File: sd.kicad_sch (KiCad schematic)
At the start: 10 parts, among them J11 microSD, Molex 104031-0811 pu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

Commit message: updoot
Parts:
- removed C66: 47u / 6.3 V X5R 0805, at the socket, Capacitor_SMD:C_0805_2012Metric, symbol Device:C
- R37: value 10k, SD_D0 pull-up -> 10k, SD_DAT0 pull-up
- R38: value 10k, SD_D1 pull-up -> 10k, SD_DAT1 pull-up
- R39: value 10k, SD_D2 pull-up -> 10k, SD_DAT2 pull-up
- R40: value 10k, SD_D3 pull-up -> 10k, SD_DAT3 pull-up
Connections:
- net SD_D0 renamed SD_DAT0
- net SD_D1 renamed SD_DAT1
- net SD_D2 renamed SD_DAT2
- net SD_D3 renamed SD_DAT3
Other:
- note added: "BOARD 3 - J11 MICROSD: PIO + DMA NATIVE 4-BIT SD. VDD = V3V3_SYS; 10k pull-ups on CMD, DAT0-DAT3 and card detect. No clock pull."
- note added: "J11: DET_A to GND and DET_B to SD_DET with a 10k pull-up, so the input reads low with a card inserted. The shield goes to GND. 100 nF + 10 uF (C64/C65) sit at the socket (DESIGN_SPEC "Rails": SD transients stay on the buck rail); the 47 uF C66 that used to be the third one is removed - a 200 mA write burst on a rail the AP63203 holds with 44 uF nominal of its own COUT does not need an 0805 bulk c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"
- note added: "Native SD GPIOs: CLK 26 (through R58, 22 ohm); CMD 27; DAT0-DAT3 28-31. All six signals are in the GPIO16-31 overlap of both PIO windows. R58 is on the MCU sheet: place physically next to U20 GPIO26. Tune 0-33 ohm if needed. Keep the bus short and direct over continuous GND, away from switching/high-current copper."
- note removed: "BOARD 3 - J11 MICROSD, LATCHED PUSH-PUSH, WIRED FOR 4-BIT PIO (also SPI-compatible). VDD = V3V3_SYS with 100 nF + 10 uF + 47 uF at the socket; 10k idle pull-ups on CMD, DAT0-3 and card detect."
- note removed: "J11: DET_A to GND and DET_B to SD_DET with a 10k pull-up, so the input reads low with a card inserted. The shield goes to GND. 100 nF + 10 uF + 47 uF sit at the socket (DESIGN_SPEC "Rails": SD transients stay on the buck rail). 10k pull-ups on CMD and DAT0-DAT3 are the SD-standard idle bias and also keep DAT3/CD high for 4-bit mode. VDD = V3V3_SYS."

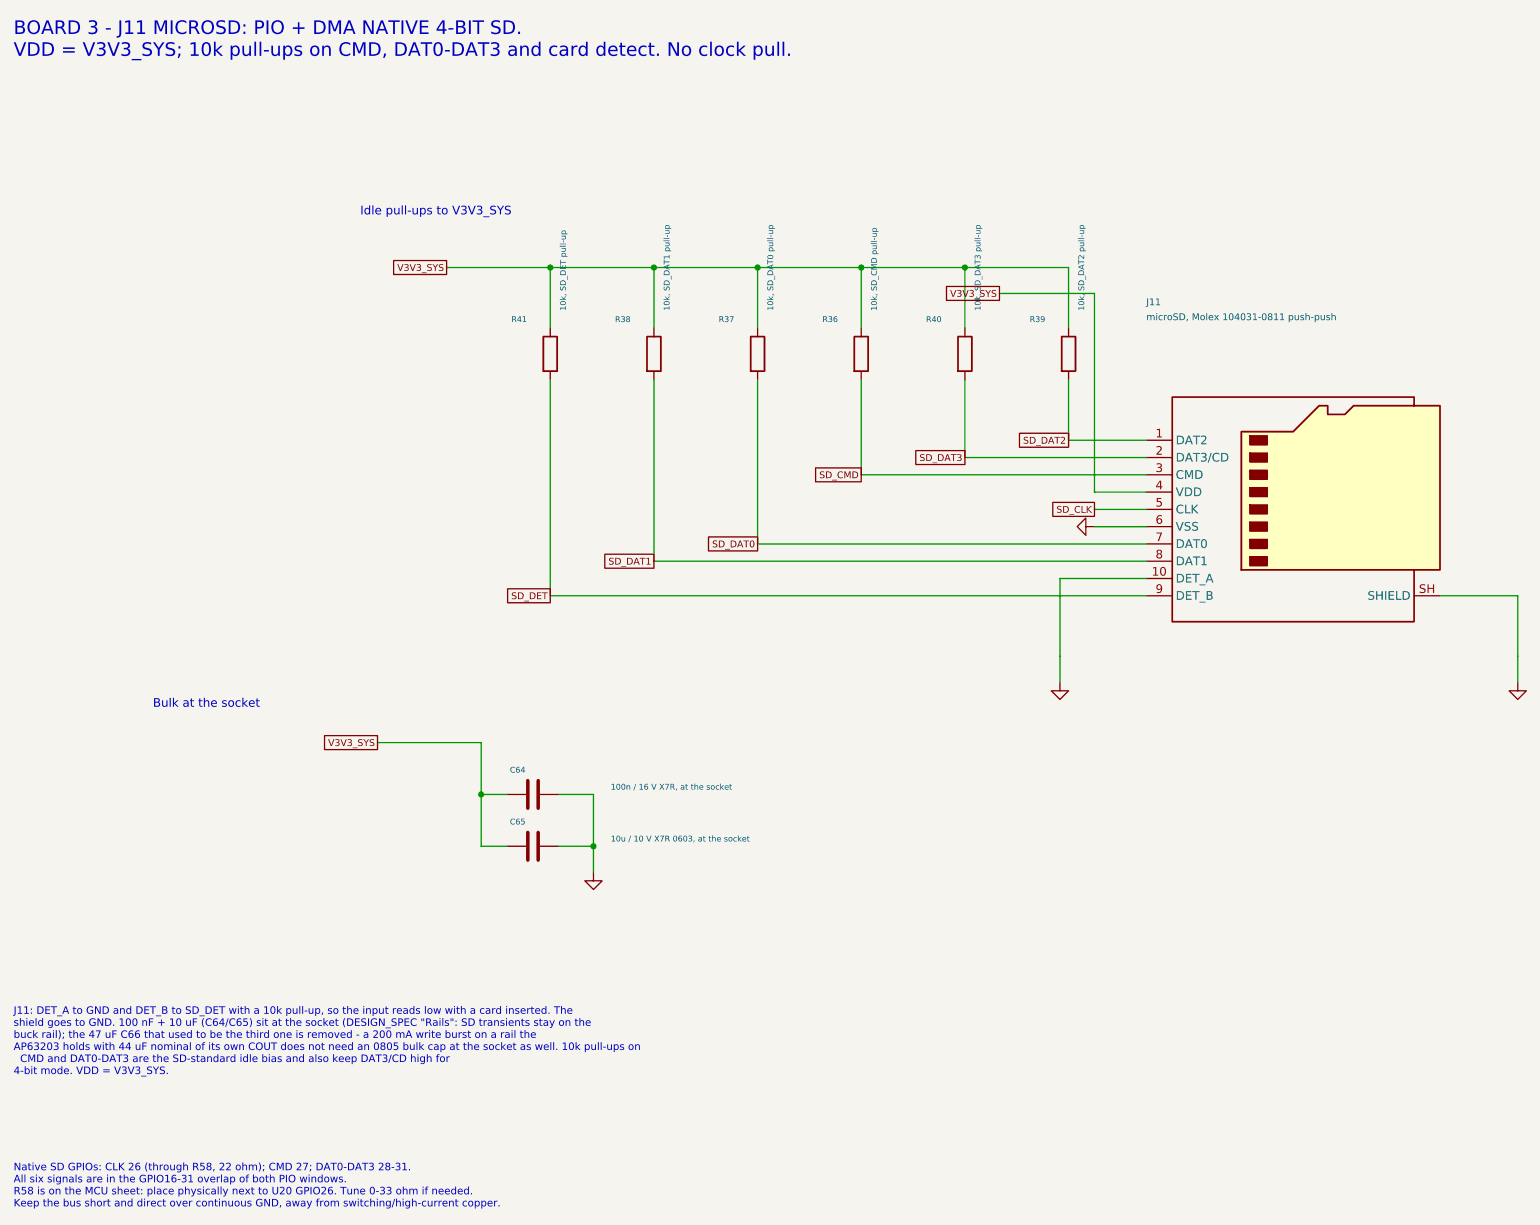
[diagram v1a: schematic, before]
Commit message: Save communication schematic, locking microSD and manual PCB updates
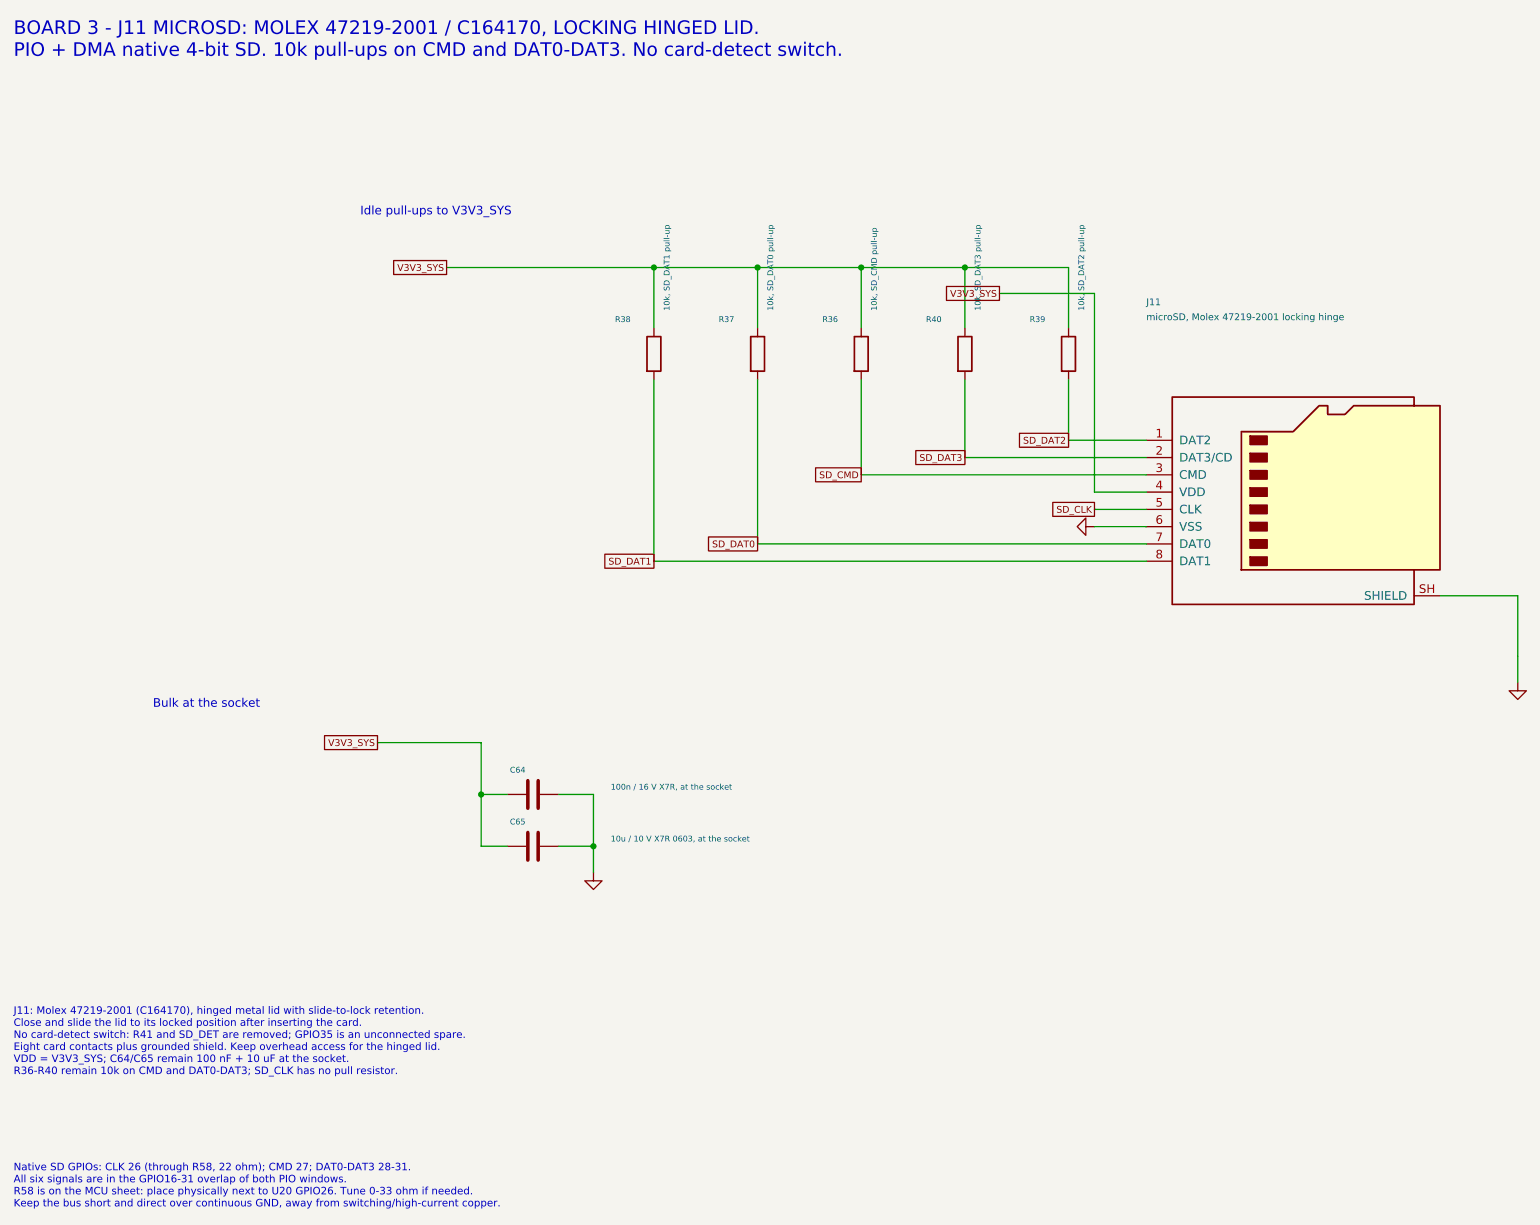
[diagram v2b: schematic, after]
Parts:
- removed R41: 10k, SD_DET pull-up, Resistor_SMD:R_0402_1005Metric, symbol Device:R
- J11: value microSD, Molex 104031-0811 push-push -> microSD, Molex 47219-2001 locking hinge; footprint MARV_Packages:microSD_HC_Molex_104031-0811 -> MARV_Packages:microSD_HC_Molex_47219-2001; symbol Connector:Micro_SD_Card_Det2 -> Connector:Micro_SD_Card; LCSC C585350 -> C164170
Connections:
- net GND: no longer J11.10 (DET_A)
- removed net SD_DET: J11.9 (DET_B)
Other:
- note added: "BOARD 3 - J11 MICROSD: MOLEX 47219-2001 / C164170, LOCKING HINGED LID. PIO + DMA native 4-bit SD. 10k pull-ups on CMD and DAT0-DAT3. No card-detect switch."
- note added: "J11: Molex 47219-2001 (C164170), hinged metal lid with slide-to-lock retention. Close and slide the lid to its locked position after inserting the card. No card-detect switch: R41 and SD_DET are removed; GPIO35 is an unconnected spare. Eight card contacts plus grounded shield. Keep overhead access for the hinged lid. VDD = V3V3_SYS; C64/C65 remain 100 nF + 10 uF at the socket. R36-R40 remain 10k 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"
- note removed: "BOARD 3 - J11 MICROSD: PIO + DMA NATIVE 4-BIT SD. VDD = V3V3_SYS; 10k pull-ups on CMD, DAT0-DAT3 and card detect. No clock pull."
- note removed: "J11: DET_A to GND and DET_B to SD_DET with a 10k pull-up, so the input reads low with a card inserted. The shield goes to GND. 100 nF + 10 uF (C64/C65) sit at the socket (DESIGN_SPEC "Rails": SD transients stay on the buck rail); the 47 uF C66 that used to be the third one is removed - a 200 mA write burst on a rail the AP63203 holds with 44 uF nominal of its own COUT does not need an 0805 bulk c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"
